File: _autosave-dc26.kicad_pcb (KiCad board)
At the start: 4 copper layers, 129.2 x 142.3 mm, 639 parts, among them U1 STM32F405RGTx

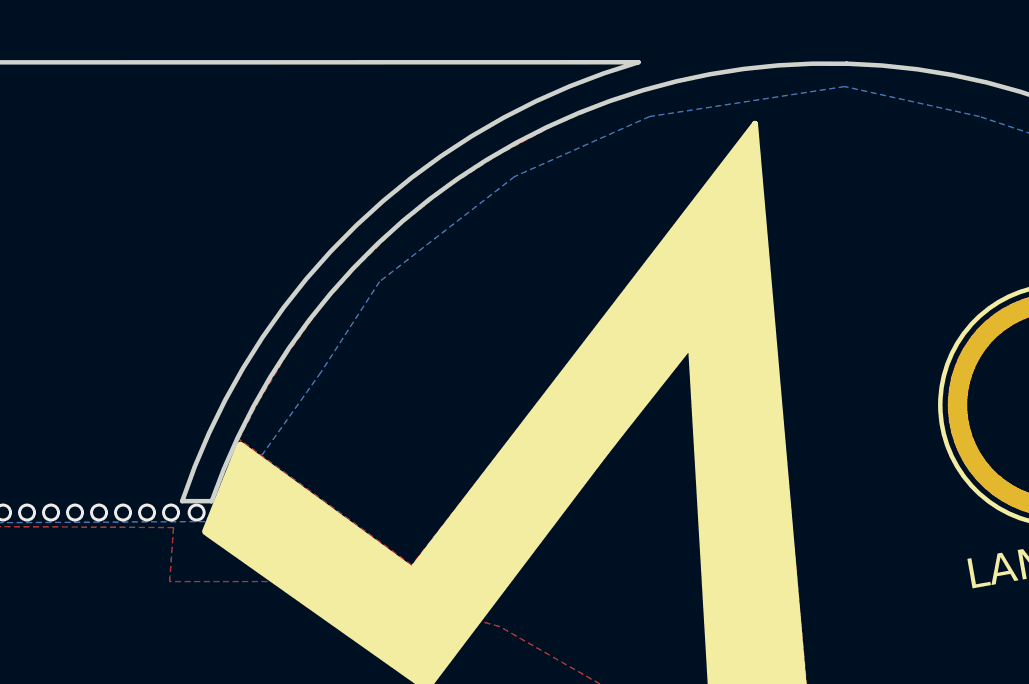
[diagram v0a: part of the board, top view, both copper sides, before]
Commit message: Top cutout + mpu6000 + spi connections
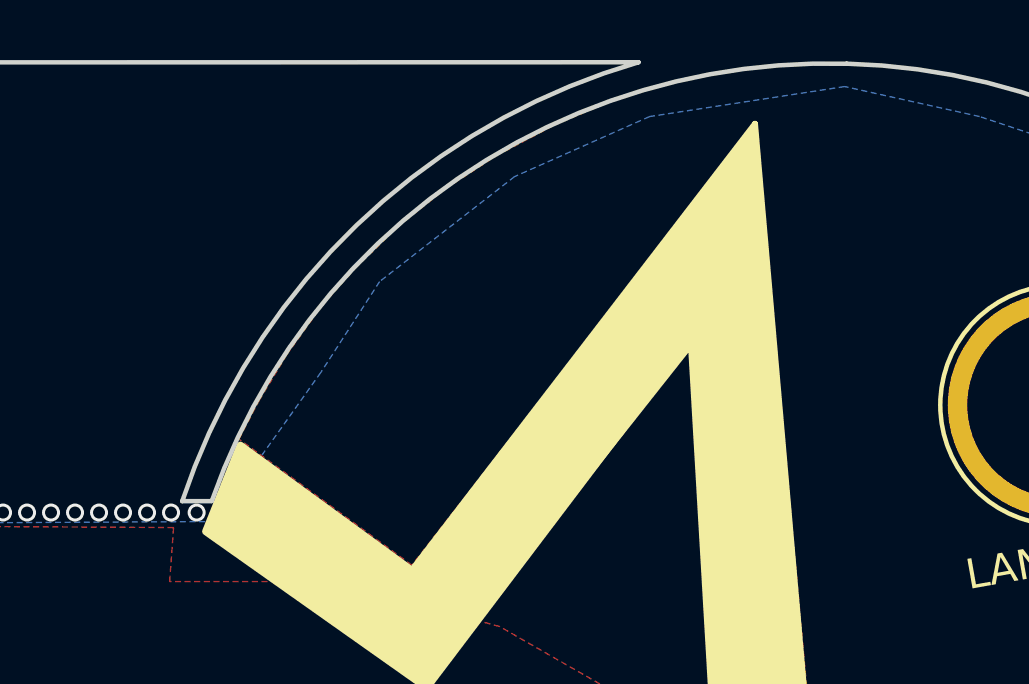
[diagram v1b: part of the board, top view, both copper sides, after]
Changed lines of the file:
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@@
     (links 2452)
     (no_connects 30)
-    (area 110.421207 55.162908 239.778793 197.578793)
+    (area 110.421207 55.114999 239.778793 197.578793)
     (thickness 1.6)
     (drawings 32)
@@
   )
   (gr_line (start 156.18 69.9) (end 194 69.9) (layer Dwgs.User) (width 0.15))
-  (gr_arc (start 214.44844 76.993044) (end 215.07 55.24) (angle -72.41097168) (layer Edge.Cuts) (width 0.15))
-  (gr_line (start 193.89 69.82) (end 192.92 69.82) (layer Edge.Cuts) (width 0.15))
+  (gr_arc (start 214.44844 76.993044) (end 215.07 55.24) (angle -72.37746534) (layer Edge.Cuts) (width 0.15))
+  (gr_line (start 193.9 69.82) (end 192.92 69.82) (layer Edge.Cuts) (width 0.15))
   (gr_arc (start 214.460753 76.993044) (end 208.13 55.19) (angle -55.39107257) (layer Edge.Cuts) (width 0.15))
   (gr_arc (start 135.669247 77.003044) (end 142 55.2) (angle 55.39107257) (layer Edge.Cuts) (width 0.15))

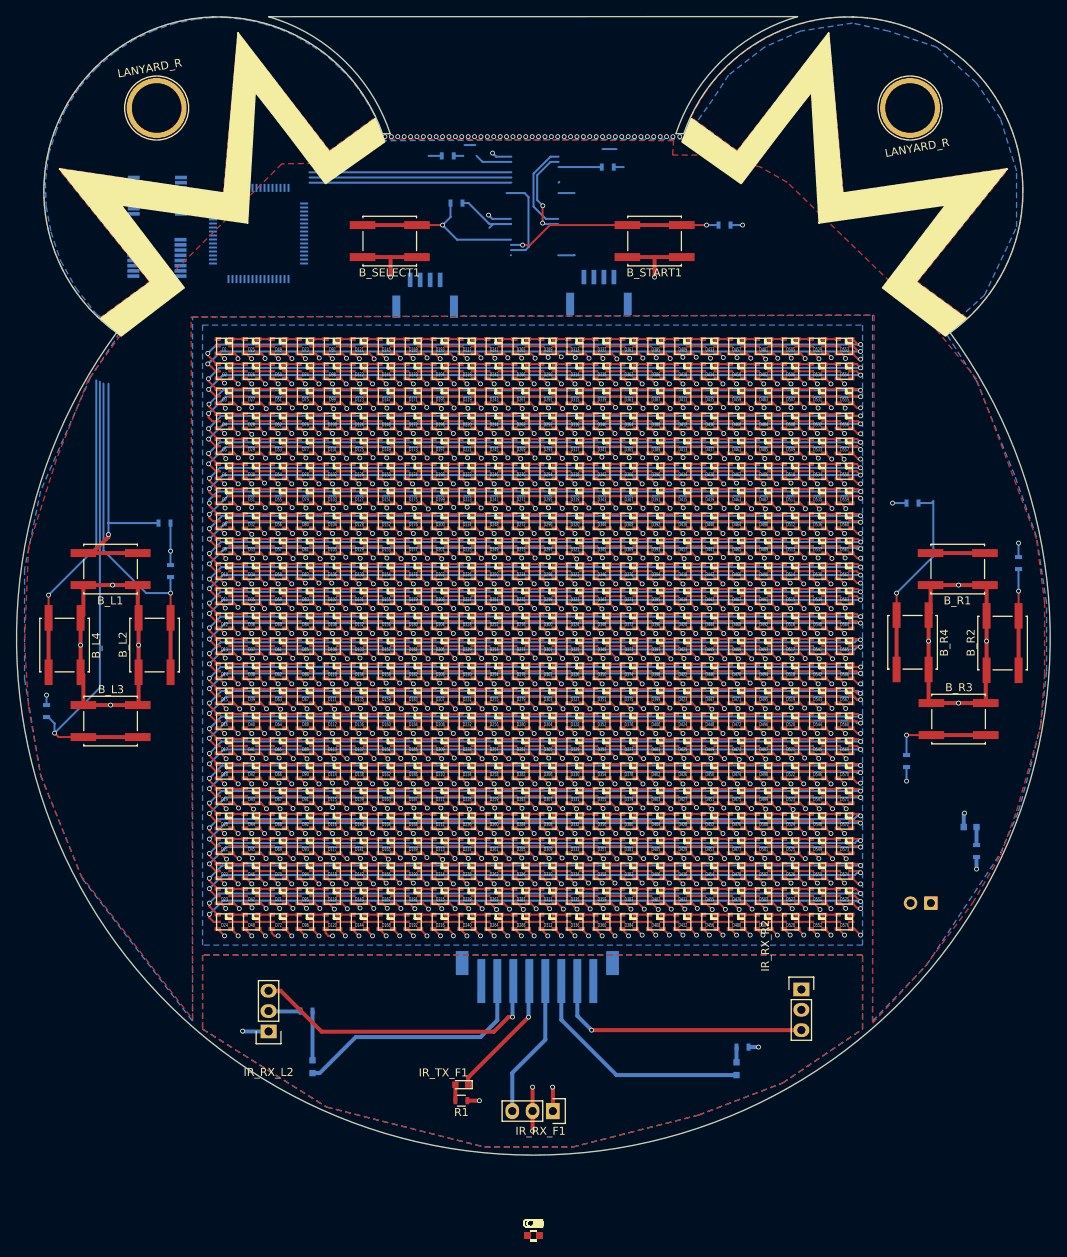
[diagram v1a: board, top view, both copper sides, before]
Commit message: moved ICs to top left and connected pins
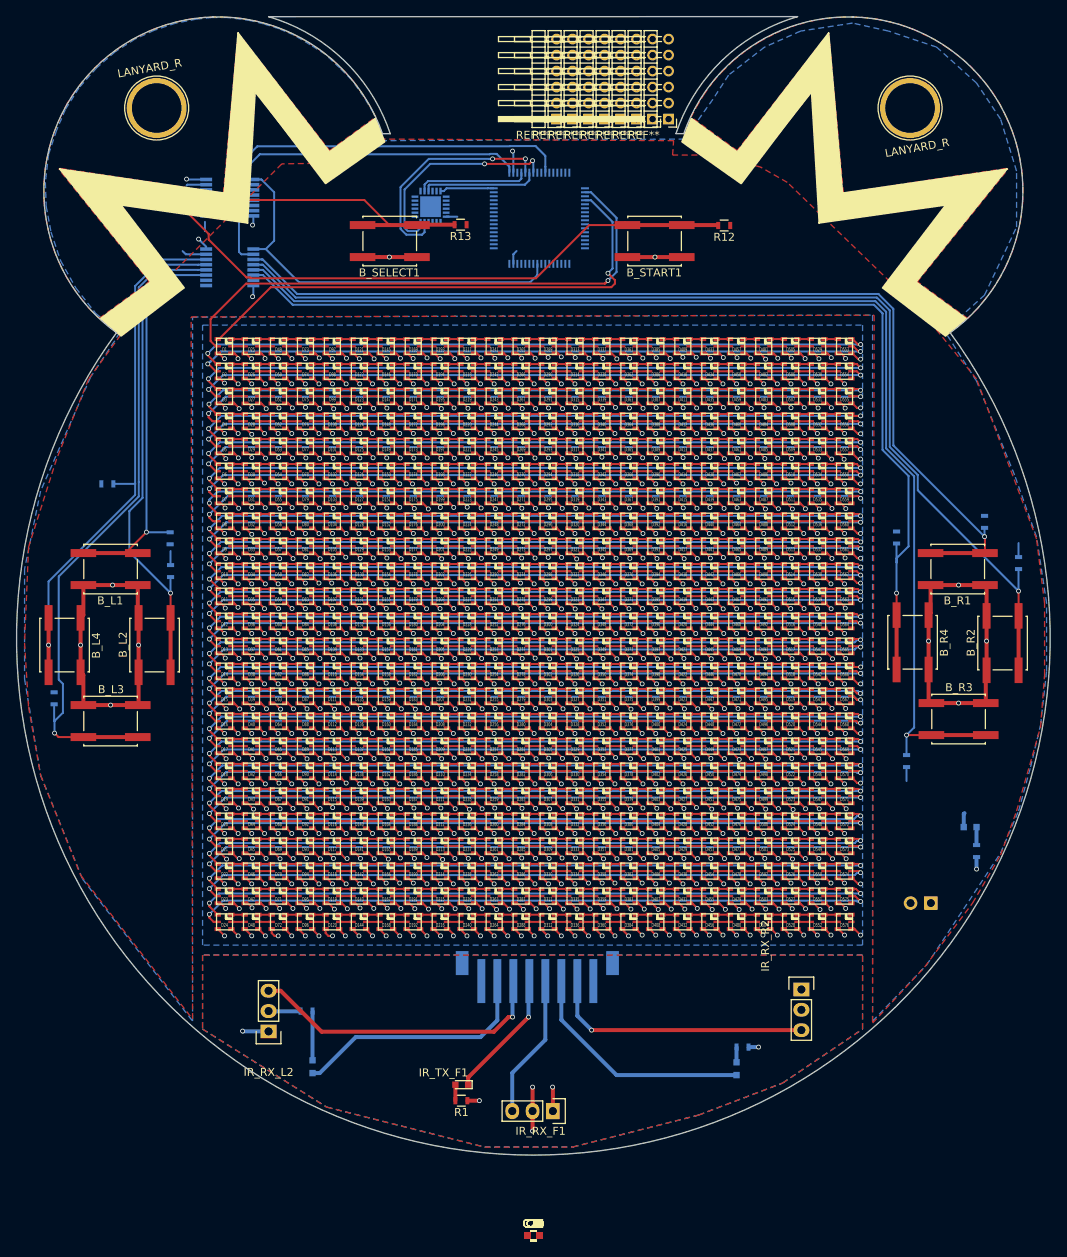
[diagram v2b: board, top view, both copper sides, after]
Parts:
- removed CON_BTNS1, CON_LEDS1: CONN_01X04, Connectors_JST:JST_GH_BM04B-GHS-TBT_04x1.25mm_Straight
- added REF**: Pin_Header_Angled_1x06_Pitch2.00mm, Pin_Headers:Pin_Header_Angled_1x06_Pitch2.00mm, F.Cu at (178.0, 68.0)
- added REF**: Pin_Header_Angled_1x06_Pitch2.00mm, Pin_Headers:Pin_Header_Angled_1x06_Pitch2.00mm, F.Cu at (180.0, 68.0)
- added REF**: Pin_Header_Angled_1x06_Pitch2.00mm, Pin_Headers:Pin_Header_Angled_1x06_Pitch2.00mm, F.Cu at (182.0, 68.0)
- added REF**: Pin_Header_Angled_1x06_Pitch2.00mm, Pin_Headers:Pin_Header_Angled_1x06_Pitch2.00mm, F.Cu at (184.0, 68.0)
- added REF**: Pin_Header_Angled_1x06_Pitch2.00mm, Pin_Headers:Pin_Header_Angled_1x06_Pitch2.00mm, F.Cu at (186.0, 68.0)
- added REF**: Pin_Header_Angled_1x06_Pitch2.00mm, Pin_Headers:Pin_Header_Angled_1x06_Pitch2.00mm, F.Cu at (188.0, 68.0)
- added REF**: Pin_Header_Angled_1x06_Pitch2.00mm, Pin_Headers:Pin_Header_Angled_1x06_Pitch2.00mm, F.Cu at (190.0, 68.0)
- added REF**: Pin_Header_Angled_1x06_Pitch2.00mm, Pin_Headers:Pin_Header_Angled_1x06_Pitch2.00mm, F.Cu at (192.0, 68.0)
- added U2: MPU-6000, Housings_DFN_QFN:QFN-24-1EP_4x4mm_Pitch0.5mm, B.Cu at (162.2, 79.0)
- R12, R13: moved to F.Cu
- moved R8 64.7 mm to (231.5, 118.3), turned to 270 degrees
- moved R7 59.1 mm to (121.8, 113.6)
- moved U1 35.2 mm to (175.8, 80.4)
- moved B_SHIFT_1 12.7 mm to (137.2, 86.5)
- moved B_SHIFT_2 11.8 mm to (137.2, 77.8)
- moved R11 4.74 mm to (220.5, 120.3), turned to 270 degrees
- moved R13 2.75 mm to (166.0, 81.2)
- moved R4 2.02 mm to (129.7, 120.4), turned to 90 degrees
- moved R6 1.86 mm to (115.2, 140.4)
- moved R12 0.07 mm to (198.9, 81.3)
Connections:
- U1 pad 17: Net-(U1-Pad17) -> Net-(B_SHIFT_1-Pad2)
- U1 pad 19: VCC -> +3V3
- U1 pad 26: Net-(U1-Pad26) -> Net-(B_SHIFT_2-Pad9)
- U1 pad 32: Net-(U1-Pad32) -> +3V3
- U1 pad 34: Net-(U1-Pad34) -> Net-(CON_LEDS1-Pad1)
- U1 pad 36: Net-(U1-Pad36) -> Net-(CON_LEDS1-Pad2)
- U1 pad 48: VCC -> +3V3
- U1 pad 57: Net-(U1-Pad57) -> Net-(B_SHIFT_1-Pad1)
- U1 pad 64: VCC -> +3V3
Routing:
- net Net-(B_R3-Pad2): track 12.4 -> 148.4 mm
- net Net-(B_R2-Pad2): track 12.7 -> 136.3 mm
- net Net-(B_R1-Pad2): track 12.2 -> 125.7 mm, vias 0 -> 1
- net Net-(B_R4-Pad2): track 25.0 -> 129.5 mm
- net Net-(CON_LEDS1-Pad1): track 0.25 -> 69.1 mm, vias 0 -> 1
- net Net-(CON_LEDS1-Pad2): track 0.00 -> 65.4 mm, vias 0 -> 1
- net Net-(B_SHIFT_2-Pad11): track 27.3 -> 79.0 mm, vias 2 -> 1
- net Net-(B_SHIFT_2-Pad9): track 0.04 -> 50.6 mm
- net Net-(B_SHIFT_1-Pad2): track 11.6 -> 50.0 mm, vias 2 -> 0
- net Net-(B_SHIFT_1-Pad1): track 11.8 -> 49.8 mm
- net Net-(B_L4-Pad2): track 40.2 -> 69.1 mm
- net Net-(U1-Pad21): track 0.00 -> 28.7 mm, vias 0 -> 2
- net Net-(U1-Pad23): track 0.00 -> 26.9 mm, vias 0 -> 2
- net Net-(B_SELECT1-Pad2): track 22.8 -> 43.4 mm
- net GND: track 742.5 -> 725.0 mm, vias 587 -> 583
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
